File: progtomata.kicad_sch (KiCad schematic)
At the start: 26 parts, among them P1 USB_C_Plug_USB2.0, SW1 SW_SPDT, U1 STM32F407VGTx, U2 AMS1117-3.3, Y1 8MHz

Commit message: Update schematics
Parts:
- added J1, J2: Conn_01x04_Pin, Connector_PinHeader_2.54mm:PinHeader_1x04_P2.54mm_Vertical, symbol Connector:Conn_01x04_Pin
- C1, C10, C11, C12, C2, C3, C4, C5, C6, C7, C9: footprint (none) -> Capacitor_SMD:C_0402_1005Metric
- C13, C14: value 12p -> 10p; footprint (none) -> Capacitor_SMD:C_0402_1005Metric
- C15, C16: footprint (none) -> Capacitor_SMD:C_0805_2012Metric
- C8: footprint (none) -> Capacitor_SMD:C_0603_1608Metric
- D1: value LED -> GREEN; footprint (none) -> LED_SMD:LED_0402_1005Metric
- FB1: footprint (none) -> Inductor_SMD:L_0603_1608Metric
- P1: footprint (none) -> Connector_USB:USB_C_Plug_Molex_105444
- R1, R2, R3: footprint (none) -> Resistor_SMD:R_0402_1005Metric
- SW1: footprint (none) -> Button_Switch_THT:SW_E-Switch_EG1224_SPDT_Angled
- Y1: footprint (none) -> Crystal:Crystal_SMD_3225-4Pin_3.2x2.5mm
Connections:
- net +3.3V: now also J1.1 (Pin_1), J2.1 (Pin_1)
- net GND: now also J1.4 (Pin_4), J2.4 (Pin_4)
- net SWCLK: now also J1.3 (Pin_3)
- net SWDIO: now also J1.2 (Pin_2)
- net UART_RX: now reaches U1.25 (PA2)
- net UART_RX: now also J2.2 (Pin_2)
- net UART_TX: now reaches U1.26 (PA3)
- net UART_TX: now also J2.3 (Pin_3)
- no-connect marks 83 -> 79
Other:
- note added: "100nF cap. for each VDD pin"
- note added: "VBUS from USB connector (+5V nominal) Minimum 22uF in/ out capacitors"
- note added: "VDDA filtering"
- moved on the sheet: C1, C10, C11, C12, C13, C14, C15, C16, C2, C3, C4, C5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

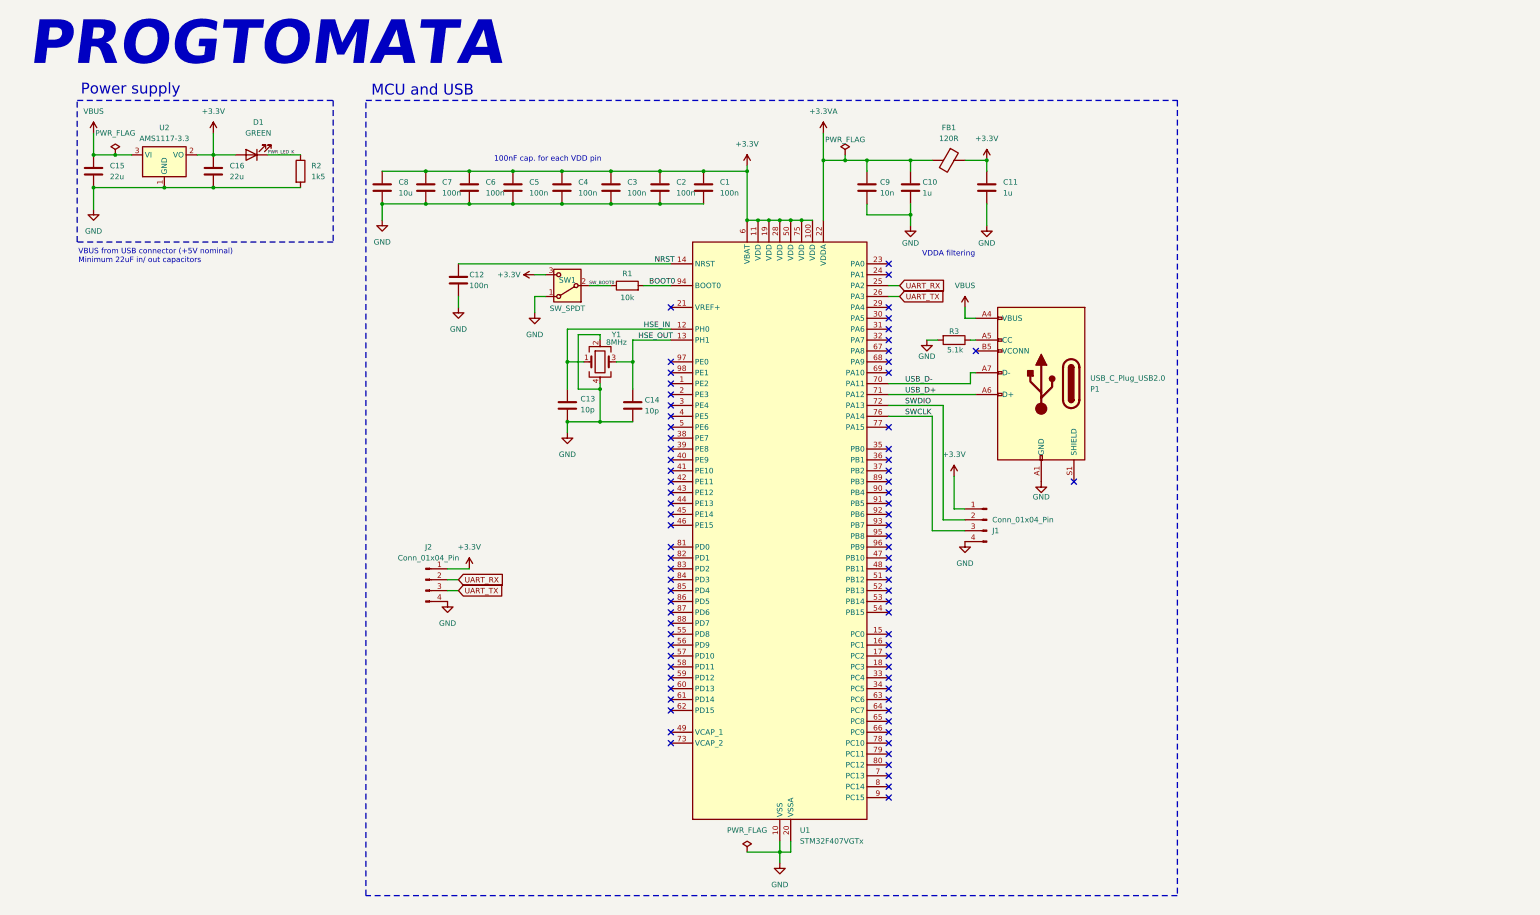
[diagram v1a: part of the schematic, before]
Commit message: Add 8-bit priority encoder
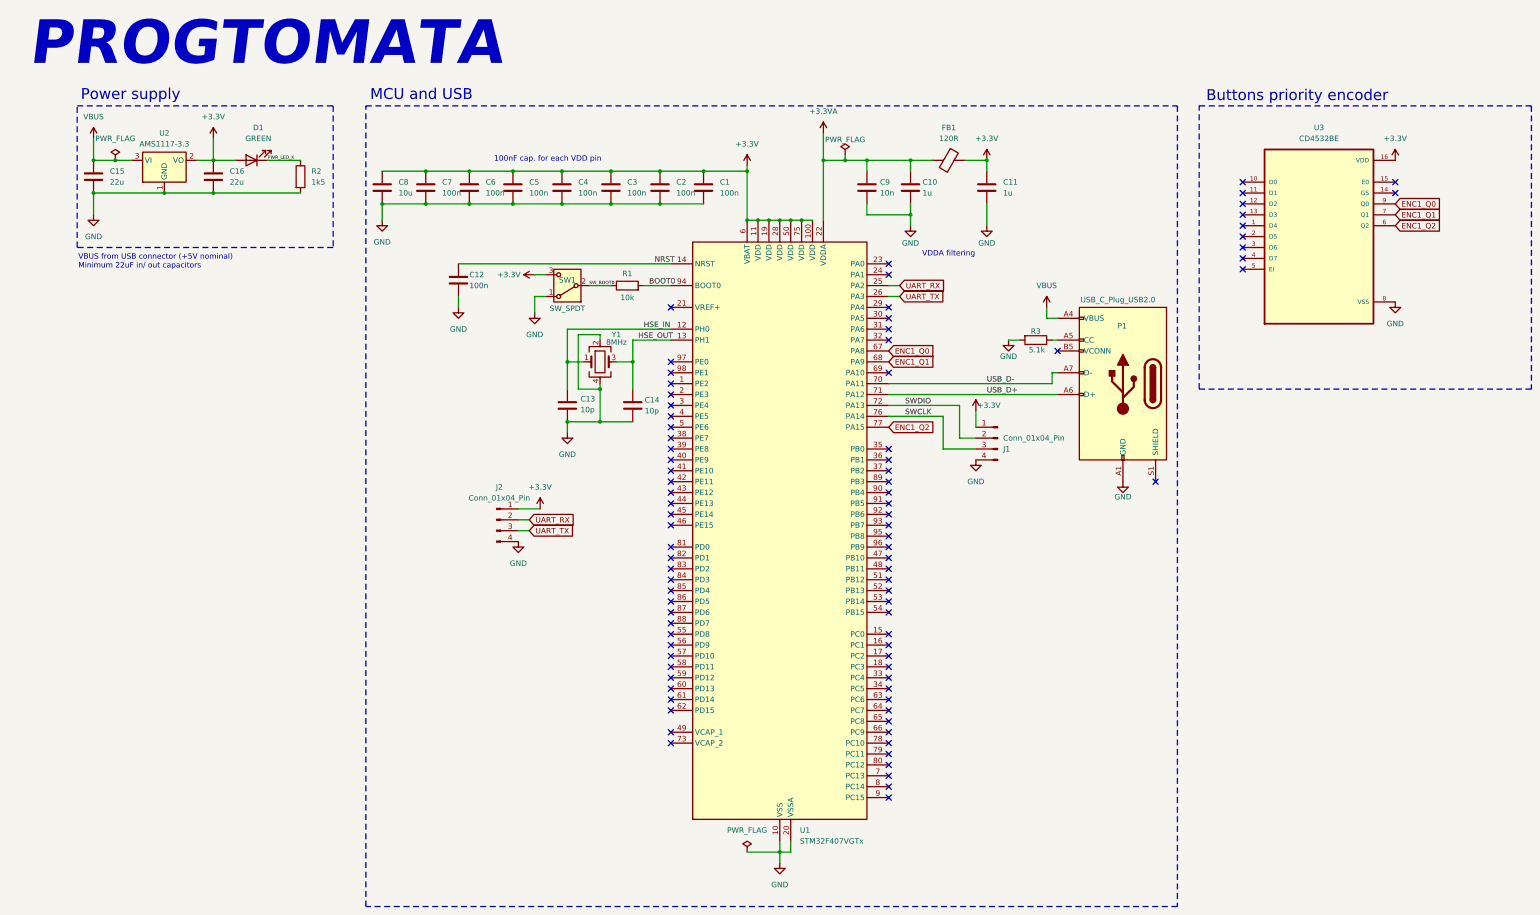
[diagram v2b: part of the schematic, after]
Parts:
- added U3: CD4532BE, CD4532BE:DIP794W45P254L1969H508Q16, symbol CD4532BE:CD4532BE
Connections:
- net +3.3V: now also U3.16 (VDD)
- net GND: now also U3.8 (VSS)
- net ENC1_Q0: now reaches U1.67 (PA8)
- net ENC1_Q0: now also U3.9 (Q0)
- net ENC1_Q1: now reaches U1.68 (PA9)
- net ENC1_Q1: now also U3.7 (Q1)
- net ENC1_Q2: now reaches U1.77 (PA15)
- net ENC1_Q2: now also U3.6 (Q2)
- no-connect marks 79 -> 87
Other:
- note added: "Buttons priority encoder"
- moved on the sheet: C15, C16, D1, J1, J2, P1, R2, R3, U2

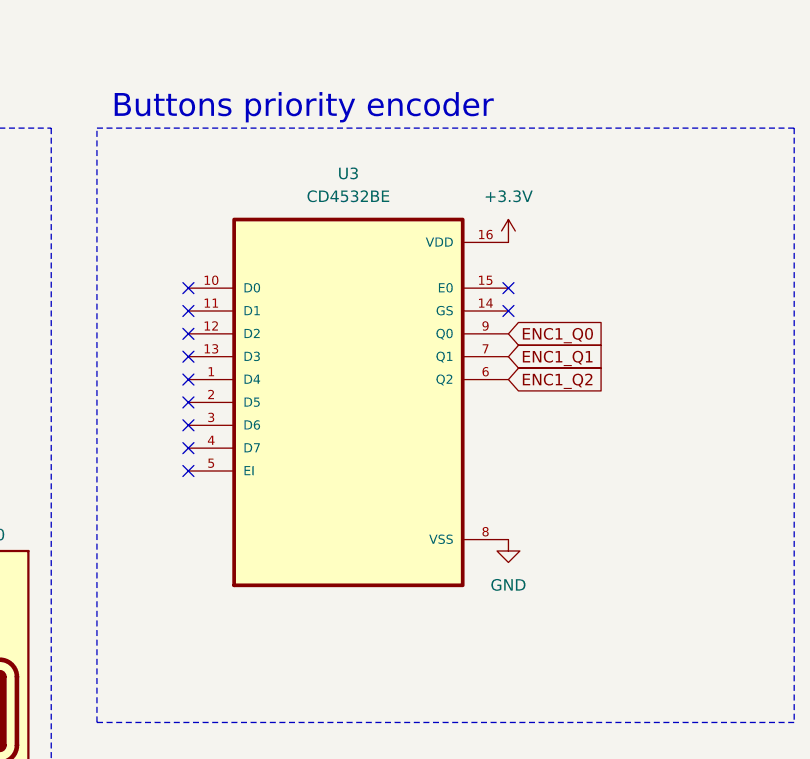
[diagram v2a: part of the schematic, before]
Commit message: Change priority encoder footprint
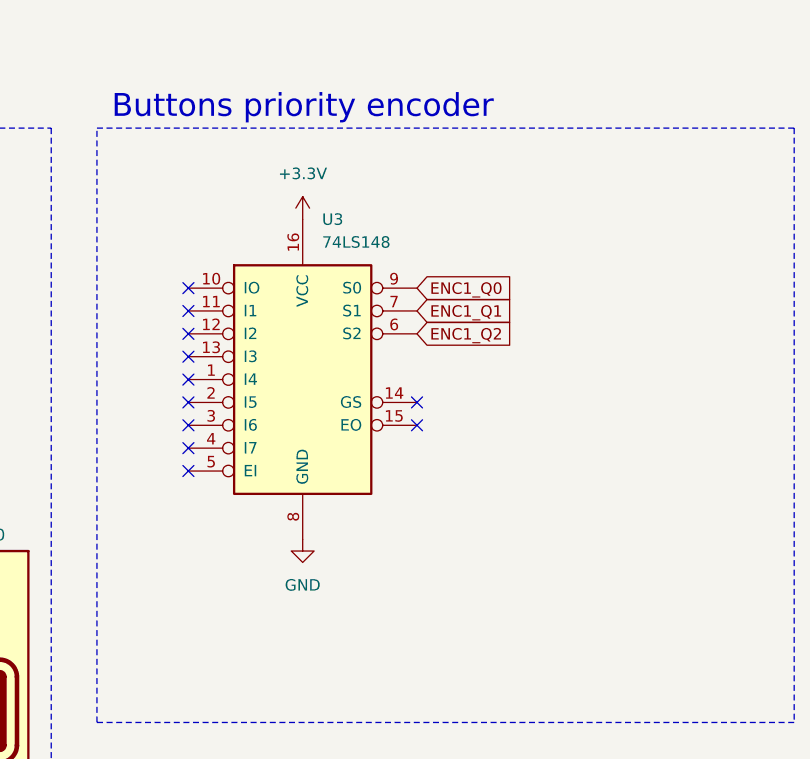
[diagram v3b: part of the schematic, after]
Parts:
- removed U3: CD4532BE, CD4532BE:DIP794W45P254L1969H508Q16, symbol CD4532BE:CD4532BE
- added U3: 74LS148, 74148:SO16, symbol 74xx:74LS148
- P1: footprint Connector_USB:USB_C_Plug_Molex_105444 -> Connector_USB:USB_C_Receptacle_GCT_USB4105-xx-A_16P_TopMnt_Horizontal
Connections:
- net +3.3V: now also U3.16 (VCC)
- net ENC1_Q0: now also U3.9 (S0)
- net ENC1_Q1: now also U3.7 (S1)
- net ENC1_Q2: now also U3.6 (S2)
- net GND: now also U3.8 (GND)

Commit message: Update PCB footprint (USB-C port, button priority encoder)
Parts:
- U3: footprint 74148:SO16 -> 74LS148:SO16
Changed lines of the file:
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@@
 			)
 		)
-		(property "Footprint" "74148:SO16"
+		(property "Footprint" "74LS148:SO16"
 			(at 302.26 66.04 0)
 			(effects

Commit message: Add button interface
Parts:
- added SW10, SW11, SW12, SW13, SW14, SW15, SW16, SW17, SW2, SW3, SW4, SW5, SW6, SW7, SW8, SW9: SW_Push_LED, Button_Switch_SMD:SW_Push_1P1T_NO_CK_PTS125Sx43PSMTR, symbol Switch:SW_Push_LED
- added U4: 74LS148, 74LS148:SO16, symbol 74xx:74LS148
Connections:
- net +3.3VA is gone; now on net +5V: C10.1, C9.1, FB1.2, U1.22 (VDDA)
- net GND: now also U4.8 (GND)
- net ENC2_Q0: now reaches U1.7 (PC13)
- net ENC2_Q0: now also U4.9 (S0)
- net ENC2_Q1: now reaches U1.8 (PC14)
- net ENC2_Q1: now also U4.7 (S1)
- net ENC2_Q2: now reaches U1.9 (PC15)
- net ENC2_Q2: now also U4.6 (S2)
- net ENC1_I4: now reaches U3.1 (I4)
- net ENC1_I4: now also SW6.2
- net ENC1_I0: now reaches U3.10 (IO)
- net ENC1_I0: now also SW2.2
- net ENC1_I1: now reaches U3.11 (I1)
- net ENC1_I1: now also SW3.2
- net ENC1_I2: now reaches U3.12 (I2)
- net ENC1_I2: now also SW4.2
- net ENC1_I3: now reaches U3.13 (I3)
- net ENC1_I3: now also SW5.2
- net ENC1_I5: now reaches U3.2 (I5)
- net ENC1_I5: now also SW7.2
- net ENC1_I6: now reaches U3.3 (I6)
- net ENC1_I6: now also SW8.2
- net ENC1_I7: now reaches U3.4 (I7)
- net ENC1_I7: now also SW9.2
- net +3.3V renamed +5V
- net +5V: now also SW10.1, SW11.1, SW12.1, SW13.1, SW14.1, SW15.1, SW16.1, SW17.1, SW2.1, SW3.1, SW4.1, SW5.1, SW6.1, SW7.1, SW8.1, SW9.1, U4.16 (VCC)
- new net ENC2_I0: SW10.2, U4.10 (IO)
- new net ENC2_I1: SW11.2, U4.11 (I1)
- new net ENC2_I2: SW12.2, U4.12 (I2)
- new net ENC2_I3: SW13.2, U4.13 (I3)
- new net ENC2_I4: SW14.2, U4.1 (I4)
- new net ENC2_I5: SW15.2, U4.2 (I5)
- new net ENC2_I6: SW16.2, U4.3 (I6)
- new net ENC2_I7: SW17.2, U4.4 (I7)
- no-connect marks 87 -> 111
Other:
- note added: "Buttons priority encoder (sample & steps)"
- note added: "Interface buttons (audio samples & steps)"
- note added: "UART connection port"
- note removed: "Buttons priority encoder"
- moved on the sheet: C1, C10, C11, C12, C13, C14, C2, C3, C4, C5, C6, C7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

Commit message: Update
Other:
- note added: "External clock source The two small caps form the load network for the crystal"
- note added: "Local high‑frequency energy storage; keeps digital noise off the supply"
- note added: "Power regulation"
- note added: "Power‑on reset filter (C12) Manual reset/boot‑mode switch (SW1->BOOT0) Pull‑up/down resistor (R1)"
- note removed: "Power supply"
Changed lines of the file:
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@@
 		(effects
 			(font
-				(face "Noto Sans")
+				(face "Verdana")
 				(size 10.16 10.16)
 				(thickness 0.508)
@@
 		)
 	)
-	(text "Power supply"
+	(text "Power regulation"
 		(exclude_from_sim no)
-		(at 30.226 35.56 0)
+		(at 33.274 36.068 0)
 		(effects
 			(font
@@
 		)
 	)
+	(text "External clock source\nThe two small caps form the\nload network for the crystal"
+		(exclude_from_sim no)
+		(at 125.222 109.982 0)
+		(effects
+			(font
+				(size 1.27 1.27)
+			)
+			(justify left)
+		)
+	)
+	(text "Local high‑frequency energy storage; keeps digital noise off the supply"
+		(exclude_from_sim no)
+		(at 93.98 53.594 0)
+		(effects
+			(font
+				(size 1.27 1.27)
+			)
+			(justify left)
+		)
+	)
 	(text "Buttons priority encoder (sample & steps)"
 		(exclude_from_sim no)
@@
 		)
 	)
+	(text "Power‑on reset filter (C12)\nManual reset/boot‑mode switch (SW1->BOOT0)\nPull‑up/down resistor (R1)"
+		(exclude_from_sim no)
+		(at 107.696 60.96 0)
+		(effects
+			(font
+				(size 1.27 1.27)
+			)
+			(justify left)
+		)
+	)
